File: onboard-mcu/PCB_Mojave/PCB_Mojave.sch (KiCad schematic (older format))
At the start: 10 parts

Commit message: Merging back in to master
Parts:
- added C? (x2): 4.7u, symbol Device:C
- added C? (x7): 0.1u, symbol Device:C
- added C?: 10u, symbol Device:C
- added D? (x2): LED_CRGB, symbol Device:LED_CRGB
- added FB?: Ferrite_Bead, symbol Device:Ferrite_Bead
- added R? (x6): R_US, symbol Device:R_US
- added U?: AP2114H-3.3TRG1, Package_TO_SOT_SMD:SOT-223-3_TabPin2, symbol PCB_Mojave_Lib:AP2114H-3.3TRG1
- C? (x2): value 10uF -> 10u
- C? (x2): value 0.1uF -> 0.1u
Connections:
- net labels added: +3.3V, +3.3VA, +3V3
- wire segments 21 -> 100
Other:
- note added: "1A MAX TOTAL ACROSS +5V AND +3.3V RAILS"
- note added: "8-28V INPUT"
- note added: "?"
- note removed: "AP2114H"
- moved on the sheet: C?, D?, F?, J?, U?

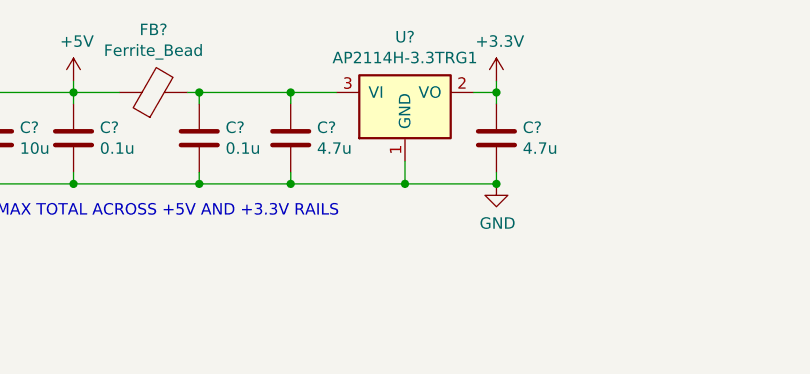
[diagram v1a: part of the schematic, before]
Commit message: Update PCB_Mojave to use Hyperlib instead of project specific library
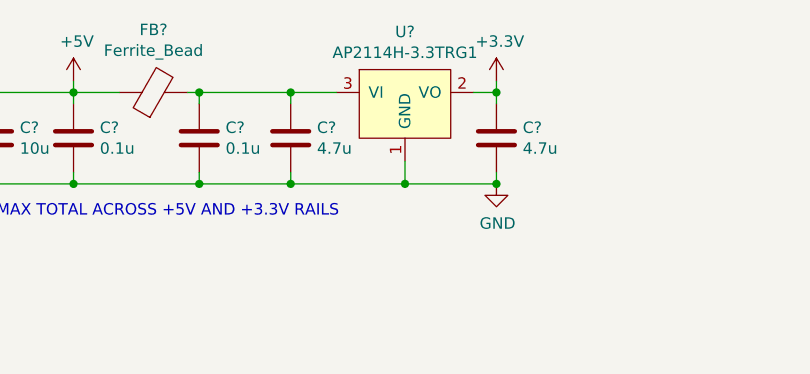
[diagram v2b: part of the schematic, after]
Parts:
- removed U?: AP2114H-3.3TRG1, Package_TO_SOT_SMD:SOT-223-3_TabPin2, symbol PCB_Mojave_Lib:AP2114H-3.3TRG1
- added U?: AP2114H-3.3TRG1, Package_TO_SOT_SMD:SOT-223-3_TabPin2, symbol Hyperlib:AP2114H-3.3TRG1
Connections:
- net +3V3: now also U?.2 (VO)
- net GND: now also U?.1 (GND)
- net at C?.1, C?.1, FB?.2: now also U?.3 (VI)
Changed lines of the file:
@@
 EESchema Schematic File Version 4
-LIBS:PCB_Mojave-cache
 EELAYER 29 0
 EELAYER END
@@
 	4150 900  4550 900
 Connection ~ 4150 900
-$Comp
-L PCB_Mojave_Lib:AP2114H-3.3TRG1 U?
-U 1 1 5ED4A91B
-P 5050 900
-F 0 "U?" H 5050 1142 50  0000 C CNN
-F 1 "AP2114H-3.3TRG1" H 5050 1051 50  0000 C CNN
-F 2 "Package_TO_SOT_SMD:SOT-223-3_TabPin2" H 5050 900 50  0001 C CNN
-F 3 "https://www.diodes.com/assets/Datasheets/AP2114.pdf" H 5050 900 50  0001 C CNN
-F 4 "https://www.digikey.com/product-detail/en/diodes-incorporated/AP2114H-3-3TRG1/AP2114H-3-3TRG1DICT-ND/4505142" H 5050 900 50  0001 C CNN "Digikey"
-F 5 "AP2114H-3.3TRG1" H 5050 900 50  0001 C CNN "Part Number"
-	1    5050 900
-	1    0    0    -1
-$EndComp
 Wire Wire Line
 	5050 1300 5050 1200
@@
 	1    0    0    -1
 $EndComp
+$Comp
+L Hyperlib:AP2114H-3.3TRG1 U?
+U 1 1 5EDF2120
+P 5050 950
+F 0 "U?" H 5050 1265 50  0000 C CNN
+F 1 "AP2114H-3.3TRG1" H 5050 1174 50  0000 C CNN
+F 2 "Package_TO_SOT_SMD:SOT-223-3_TabPin2" H 5000 1000 50  0001 C CNN
+F 3 "https://www.diodes.com/assets/Datasheets/AP2114.pdf" H 5000 1000 50  0001 C CNN
+	1    5050 950
+	1    0    0    -1
+$EndComp
